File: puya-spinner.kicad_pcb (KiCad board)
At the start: 2 copper layers, 119 x 27 mm, 51 parts, among them J1 Conn_ARM_SWD_TagConnect_TC2030, U1 PY32F002AF15P6, U2 SC7A20

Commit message: tweaks; mostly to big capacitor
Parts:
- moved C4 7.91 mm to (136.5, 98.5), turned to 90 degrees
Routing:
- net +BATT: track 139.2 -> 132.3 mm
- net GND: track 15.6 -> 9.18 mm
- net /ACCEL_SCL: track 42.7 -> 43.3 mm
- net /ACCEL_SDA: track 47.3 -> 47.9 mm

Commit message: mostly idle tweaks
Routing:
- net Net-(D1-A): track 46.9 -> 47.7 mm
- net /~{RST}: track 80.1 -> 79.5 mm
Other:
- board text added: "RX"
- board text added: "TX"

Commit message: fix bearing hole; add reverse polarity protection
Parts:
- added Q1: AO3401A, Package_TO_SOT_SMD:SOT-23, F.Cu at (138.0, 107.0)
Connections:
- BT1 pad 1: +BATT -> Net-(BT1-+)
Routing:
- net Net-(BT1-+): track 0.00 -> 10.5 mm
- net +BATT: track 132.4 -> 138.7 mm
- net GND: vias 11 -> 12

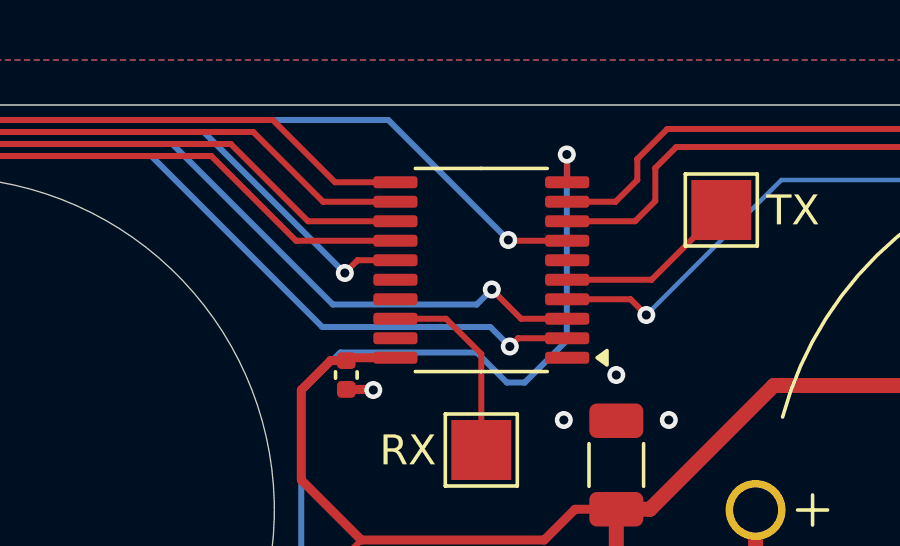
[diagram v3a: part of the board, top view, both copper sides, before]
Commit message: some tweaks to make ground plane look nicer
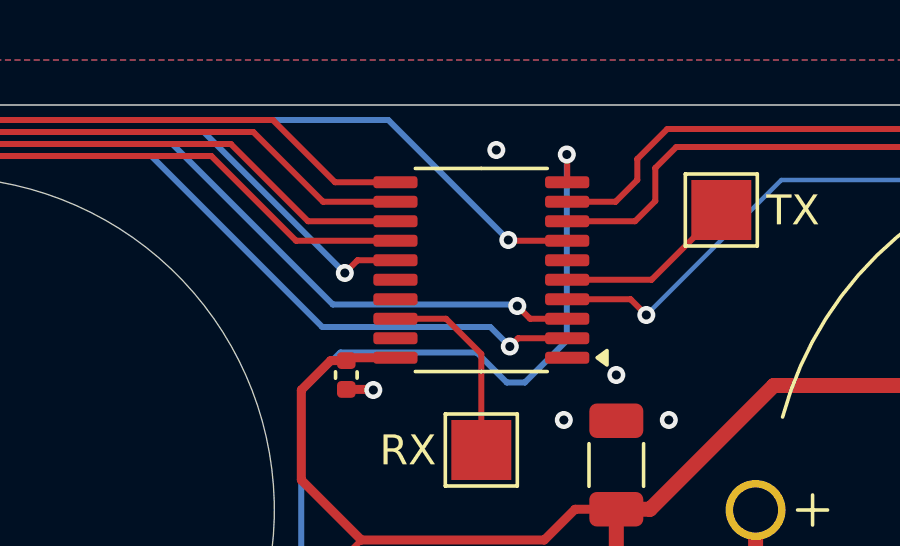
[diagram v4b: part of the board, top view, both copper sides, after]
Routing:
- net GND: vias 12 -> 13
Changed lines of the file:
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@@
+	)
+	(via
+		(at 132.5 88)
+		(size 0.6)
+		(drill 0.3)
+		(layers "F.Cu" "B.Cu")
+		(free yes)
+		(net 2)
 	)
 	(via
@@
 	)
 	(segment
-		(start 134.8625 93.625)
-		(end 133.325 93.625)
+		(start 133.625 93.625)
+		(end 134.8625 93.625)
 		(width 0.2)
 		(layer "F.Cu")
@@
 	)
 	(segment
-		(start 133.325 93.625)
-		(end 132.35 92.65)
+		(start 133.2 93.2)
+		(end 133.625 93.625)
 		(width 0.2)
 		(layer "F.Cu")
@@
 	)
 	(via
-		(at 132.35 92.65)
-		(size 0.6)
-		(drill 0.3)
-		(layers "F.Cu" "B.Cu")
+		(at 133.2 93.2)
+		(size 0.6)
+		(drill 0.3)
+		(layers "F.Cu" "B.Cu")
+		(net 12)
+	)
+	(segment
+		(start 127.05 93.15)
+		(end 121.7 87.8)
+		(width 0.2)
+		(layer "B.Cu")
+		(net 12)
+	)
+	(segment
+		(start 133.2 93.2)
+		(end 133.15 93.15)
+		(width 0.2)
+		(layer "B.Cu")
+		(net 12)
+	)
+	(segment
+		(start 95.585 92.95)
+		(end 94.635 92)
+		(width 0.2)
+		(layer "B.Cu")
+		(net 12)
+	)
+	(segment
+		(start 121.7 87.8)
+		(end 104.45 87.8)
+		(width 0.2)
+		(layer "B.Cu")
+		(net 12)
+	)
+	(segment
+		(start 99.3 92.95)
+		(end 95.585 92.95)
+		(width 0.2)
+		(layer "B.Cu")
+		(net 12)
+	)
+	(segment
+		(start 133.15 93.15)
+		(end 127.05 93.15)
+		(width 0.2)
+		(layer "B.Cu")
 		(net 12)
 	)
@@
 		(width 0.2)
 		(layer "B.Cu")
-		(net 12)
-	)
-	(segment
-		(start 95.585 92.95)
-		(end 94.635 92)
-		(width 0.2)
-		(layer "B.Cu")
-		(net 12)
-	)
-	(segment
-		(start 99.3 92.95)
-		(end 95.585 92.95)
-		(width 0.2)
-		(layer "B.Cu")
-		(net 12)
-	)
-	(segment
-		(start 132.35 92.65)
-		(end 131.85 93.15)
-		(width 0.2)
-		(layer "B.Cu")
-		(net 12)
-	)
-	(segment
-		(start 121.7 87.8)
-		(end 104.45 87.8)
-		(width 0.2)
-		(layer "B.Cu")
-		(net 12)
-	)
-	(segment
-		(start 131.85 93.15)
-		(end 127.05 93.15)
-		(width 0.2)
-		(layer "B.Cu")
-		(net 12)
-	)
-	(segment
-		(start 127.05 93.15)
-		(end 121.7 87.8)
-		(width 0.2)
-		(layer "B.Cu")

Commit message: revA for fab
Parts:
- H1: value MountingHole -> 608 bearing
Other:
- board text added: "2024-08-18"
- board text added: "PY32 POV spinner Design by @ArcaneNibble"
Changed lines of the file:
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@@
 	)
 	(paper "A4")
+	(title_block
+		(title "PY32 POV spinner demo")
+		(date "2024-08-18")
+		(rev "A")
+		(company "ArcaneNibble")
+	)
 	(layers
 		(0 "F.Cu" signal)
@@
 			(usegerberattributes yes)
 			(usegerberadvancedattributes yes)
-			(creategerberjobfile yes)
+			(creategerberjobfile no)
 			(dashed_line_dash_ratio 12.000000)
 			(dashed_line_gap_ratio 3.000000)
@@
 			(outputformat 1)
 			(mirror no)
-			(drillshape 1)
+			(drillshape 0)
 			(scaleselection 1)
-			(outputdirectory "")
+			(outputdirectory "revA")
 		)
 	)
@@
 		(tags "resistor")
 		(property "Reference" "R2"
-			(at 0 -1.17 270)
+			(at 0 -1.17 -90)
 			(layer "F.SilkS")
 			(hide yes)
@@
 		)
 		(property "Value" "10k"
-			(at 0 1.17 270)
+			(at 0 1.17 -90)
 			(layer "F.Fab")
 			(effects
@@
 		)
 		(fp_text user "${REFERENCE}"
-			(at 0 0 270)
+			(at 0 0 -90)
 			(layer "F.Fab")
 			(effects
@@
 			)
 		)
-		(property "Value" "MountingHole"
+		(property "Value" "608 bearing"
 			(at 0 1 0)
 			(unlocked yes)
@@
 		(sheetname "Root")
 		(sheetfile "puya-spinner.kicad_sch")
-		(attr exclude_from_pos_files)
+		(attr exclude_from_pos_files exclude_from_bom)
 		(fp_line
 			(start -1.2 -1.2)
@@
 		(tags "resistor")
 		(property "Reference" "R1"
-			(at 0 -1.17 360)
+			(at 0 -1.17 0)
 			(layer "F.SilkS")
 			(hide yes)
@@
 		)
 		(property "Value" "10k"
-			(at 0 1.17 360)
+			(at 0 1.17 0)
 			(layer "F.Fab")
 			(effects
@@
 		)
 		(fp_text user "${REFERENCE}"
-			(at 0 0 360)
+			(at 0 0 0)
 			(layer "F.Fab")
 			(effects
@@
 		(sheetname "Root")
 		(sheetfile "puya-spinner.kicad_sch")
-		(attr exclude_from_pos_files)
+		(attr exclude_from_pos_files exclude_from_bom)
 		(fp_line
 			(start -1.2 -1.2)
@@
 			)
 		)
+		(property "LCSC" "C2979167"
+			(at 0 0 0)
+			(unlocked yes)
+			(layer "F.Fab")
+			(hide yes)
+			(effects
+				(font
+					(size 1 1)
+					(thickness 0.15)
+				)
+			)
+		)
 		(sheetname "Root")
 		(sheetfile "puya-spinner.kicad_sch")
@@
 		(tags "net tie solder jumper bridged")
 		(property "Reference" "JP2"
-			(at 0 -1.8 270)
+			(at 0 -1.8 -90)
 			(layer "F.SilkS")
 			(hide yes)
@@
 		)
 		(property "Value" "SolderJumper_2_Bridged"
-			(at 0 1.9 270)
+			(at 0 1.9 -90)
 			(layer "F.Fab")
 			(effects
@@
 		(tags "lga land grid array")
 		(property "Reference" "U2"
-			(at 0 -2.075 270)
+			(at 0 -2.075 -90)
 			(layer "F.SilkS")
 			(hide yes)
@@
 		)
 		(property "Value" "SC7A20"
-			(at 0 1.6 270)
+			(at 0 1.6 -90)
 			(layer "F.Fab")
 			(effects
@@
 		)
 		(fp_text user "${REFERENCE}"
-			(at 0 0 270)
+			(at 0 0 -90)
 			(layer "F.Fab")
 			(effects
@@
 		(tags "capacitor")
 		(property "Reference" "C4"
-			(at 0 -1.85 270)
+			(at 0 -1.85 -90)
 			(layer "F.SilkS")
 			(hide yes)
@@
 		)
 		(property "Value" "10 uF"
-			(at 0 1.85 270)
+			(at 0 1.85 -90)
 			(layer "F.Fab")
 			(effects
@@
 		)
 		(fp_text user "${REFERENCE}"
-			(at 0 0 270)
+			(at 0 0 -90)
 			(layer "F.Fab")
 			(effects
@@
 		(tags "capacitor")
 		(property "Reference" "C1"
-			(at 0 -1.16 360)
+			(at 0 -1.16 0)
 			(layer "F.SilkS")
 			(hide yes)
@@
 		)
 		(property "Value" "0.1 uF"
-			(at 0 1.16 360)
+			(at 0 1.16 0)
 			(layer "F.Fab")
 			(effects
@@
 		)
 		(fp_text user "${REFERENCE}"
-			(at 0 0 360)
+			(at 0 0 0)
 			(layer "F.Fab")
 			(effects
@@
 		(tags "tag connect programming header pogo pins")
 		(property "Reference" "J1"
-			(at 0 -5 270)
+			(at 0 -5 -90)
 			(layer "B.SilkS")
 			(hide yes)
@@
 		)
 		(property "Value" "Conn_ARM_SWD_TagConnect_TC2030"
-			(at 0 4.7 270)
+			(at 0 4.7 -90)
 			(layer "B.Fab")
 			(hide yes)
@@
 		)
 		(fp_text user "KEEPOUT"
-			(at 0 0 270)
+			(at 0 0 -90)
 			(layer "Cmts.User")
 			(effects
@@
 					(thickness 0.07)
 				)
+				(justify mirror)
 			)
 		)
 		(fp_text user "${REFERENCE}"
-			(at 0 0 270)
+			(at 0 0 -90)
 			(layer "B.Fab")
 			(effects
@@
 		(layer "Edge.Cuts")
 	)
+	(gr_text "2024-08-18"
+		(at 145.4 107 0)
+		(layer "F.Cu")
+		(effects
+			(font
+				(size 1.5 1.5)
+				(thickness 0.3)
+				(bold yes)
+			)
+			(justify left bottom)
+		)
+	)
 	(gr_text "GND"
 		(at 83.5 90 0)
@@
 		(layer "B.SilkS")
 		(effects
+			(font
+				(size 1.5 1.5)
+				(thickness 0.15)
+			)
+			(justify left bottom mirror)
+		)
+	)
+	(gr_text "PY32 POV spinner\nDesign by @ArcaneNibble"
+		(at 164 107.5 0)
+		(layer "B.SilkS")
+		(effects
